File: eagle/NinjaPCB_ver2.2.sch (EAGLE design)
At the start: 72 parts, among them IC3 ANALOGSW_AD_SOT23-6, IC6 NAU7802, J2 ATX24, J3 HEATER, J4 HEATER_TEMP, Q1 S8550, Q2 IRF520NPBF, Q3 IRF520NPBF, Q4 S8550, Q5 IRF520NPBF, Q6 S8550, Q7 S8550, Q8 S8550, U1 CJT1117-3.3-SOT223

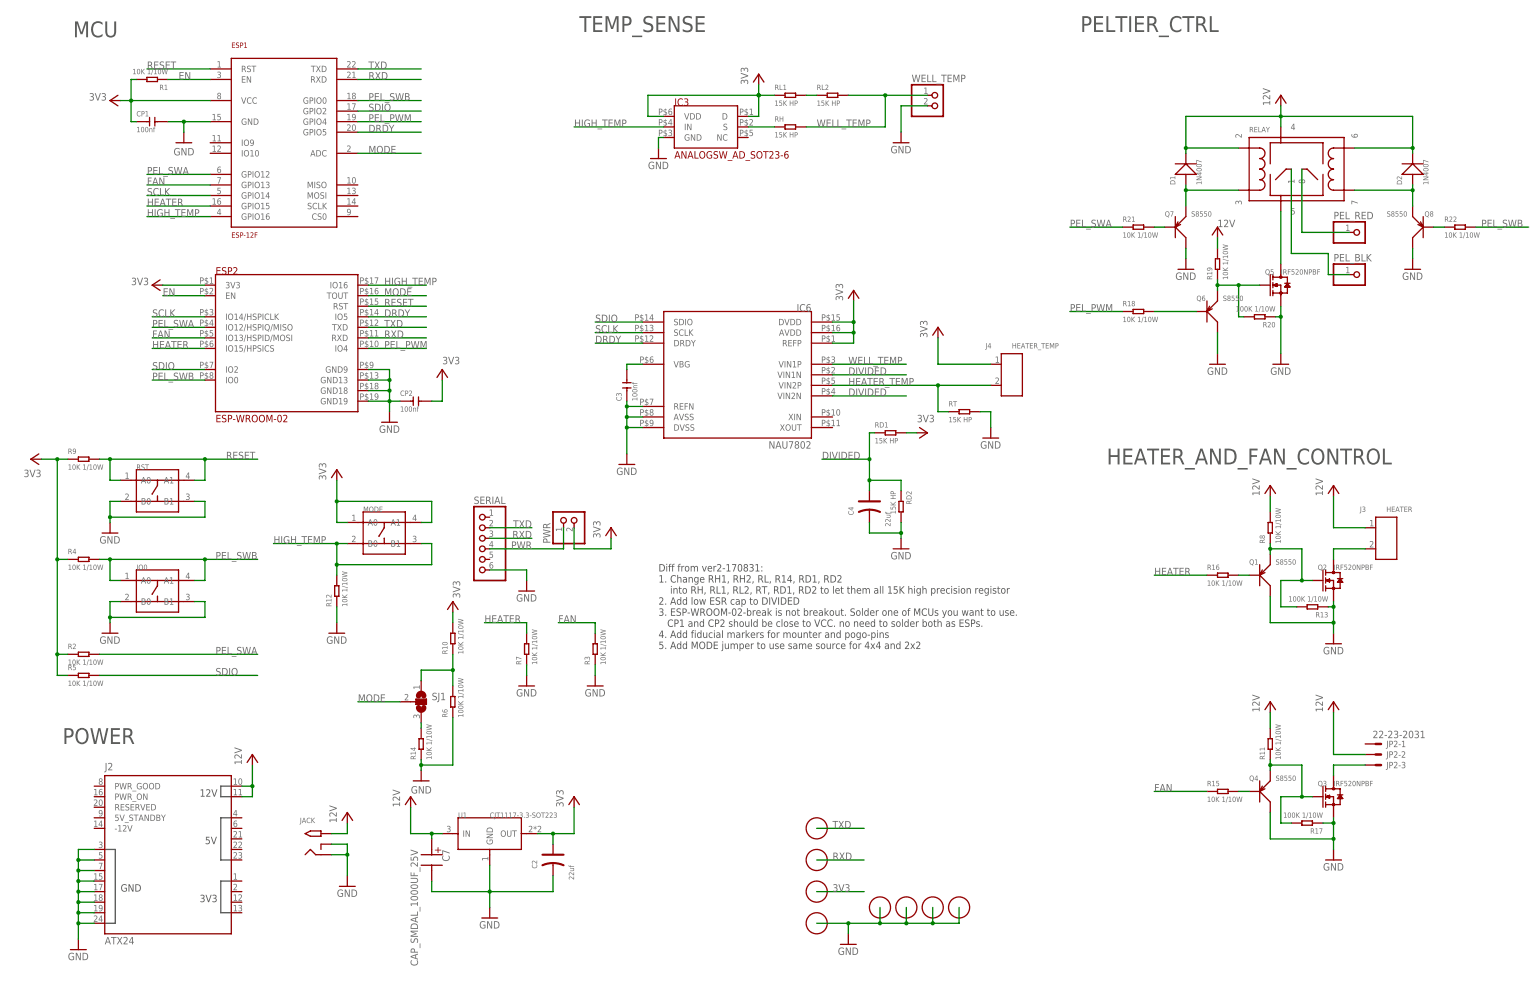
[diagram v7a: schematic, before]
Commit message: split into 2 subprojects : 4x4 NinNin and 2x2 MooMoo
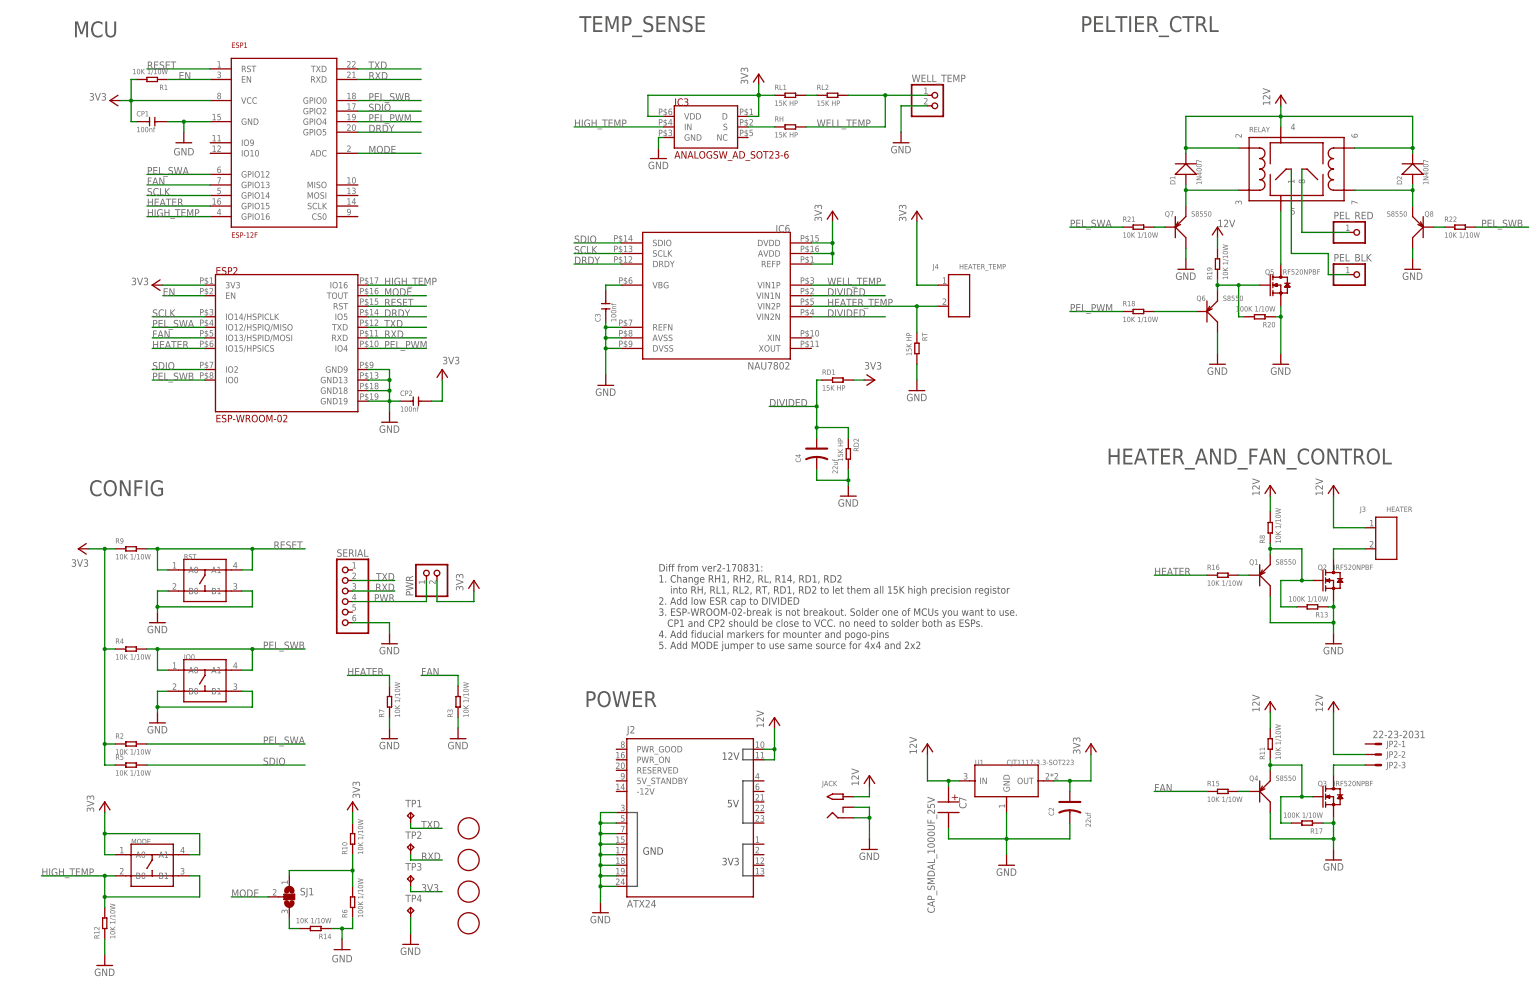
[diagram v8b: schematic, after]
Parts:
- removed U$1, U$2, U$7, U$8: FIDUCIAL, adafruit:FIDUCIAL
- added TP1, TP2, TP3, TP4: TPTP20R, testpad:TPTP20R
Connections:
- net 3V3: now also TP3.TP
- net GND: now also TP4.TP
- net RXD: now also TP2.TP
- net TXD: now also TP1.TP
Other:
- note added: "CONFIG"
- moved on the sheet: C2, C3, C4, C7, IC6, IO0, J2, J4, JACK, MODE, PWR, R10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
